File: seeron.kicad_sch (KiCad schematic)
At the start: 13 parts

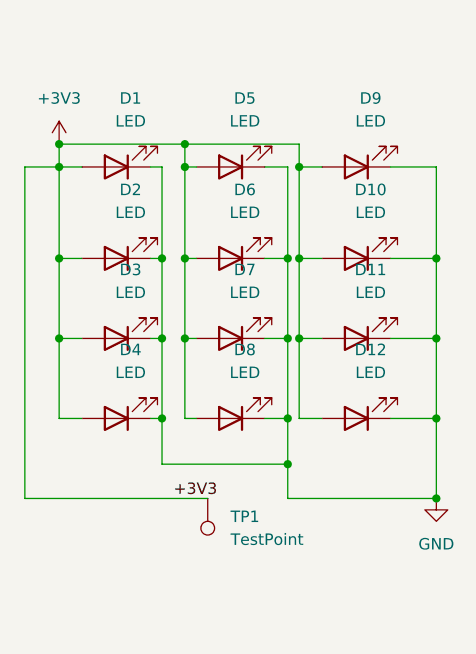
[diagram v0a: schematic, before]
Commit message: Add readme and more test points for providing power contacts if solder mask is used
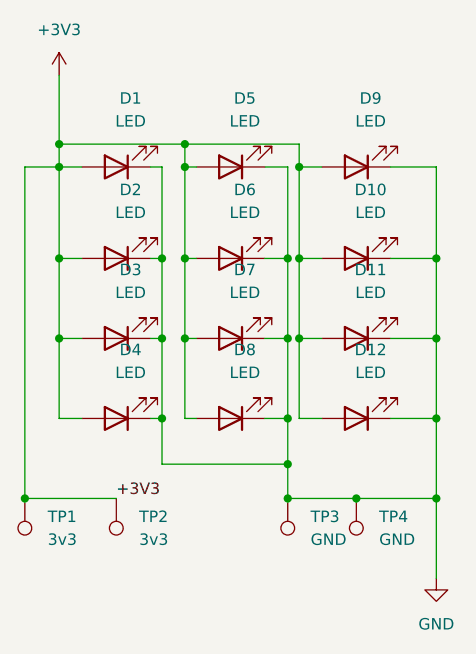
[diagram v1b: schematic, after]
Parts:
- added TP2: 3v3, TestPoint:TestPoint_Pad_D1.0mm, symbol Connector:TestPoint
- added TP3, TP4: GND, TestPoint:TestPoint_Pad_D1.0mm, symbol Connector:TestPoint
- TP1: value TestPoint -> 3v3
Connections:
- net +3V3: now also TP2.1
- net GND: now also TP3.1, TP4.1
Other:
- company: (none) -> accelerando.com.au
- title: (none) -> The Eye of Seeron
- moved on the sheet: TP1
